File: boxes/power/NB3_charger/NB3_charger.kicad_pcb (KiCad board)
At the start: 2 copper layers, 65 x 150.1 mm, 58 parts, among them J1 Barrel_Jack-DC-5.5-2.1, J2 B4B-PH-K-S, J3 Conn_01x02_Pin, J4 Conn_01x02_Pin, J5 Conn_01x02_Pin, J6 Conn_01x02_Pin, Q1 PMOS_FDC658AP, SW1 SW_SPDT, SW2 SW_SPDT, T1 NTCG163JF103FT1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

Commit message: Work on NB3 Charger wiring
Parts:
- moved T1 99.1 mm to (128.9, 101.1)
- moved C1 43.0 mm to (177.7, 38.5)
- moved C10 43.0 mm to (162.0, 40.6)
- moved C11 43.0 mm to (163.7, 37.3)
- moved C12 43.0 mm to (167.7, 47.2)
- moved C13 43.0 mm to (170.2, 47.2)
- moved C14 43.0 mm to (170.2, 51.2)
- moved C15 43.0 mm to (167.7, 51.2)
- moved C16 43.0 mm to (173.7, 52.4)
- moved C2 43.0 mm to (175.2, 38.5)
- moved C3 43.0 mm to (180.2, 38.5)
- moved C4 43.0 mm to (180.2, 42.0)
- moved C5 43.0 mm to (177.7, 42.0)
- moved C6 43.0 mm to (175.2, 42.0)
- moved C7 43.0 mm to (161.5, 42.9)
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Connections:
- BT1 pad N: Net-(BT1-PadN) -> GND
- BT1 pad P: +BATT -> Net-(BT1-PadP)
- BT2 pad N: Net-(BT2-PadN) -> Net-(BT1-PadP)
- BT2 pad P: Net-(BT1-PadN) -> Net-(BT2-PadP)
- BT3 pad N: Net-(BT3-PadN) -> Net-(BT2-PadP)
- BT3 pad P: Net-(BT2-PadN) -> Net-(BT3-PadP)
- BT4 pad N: Net-(BT4-PadN) -> Net-(BT3-PadP)
- BT4 pad P: Net-(BT3-PadN) -> Net-(BT4-PadP)
- BT5 pad N: Net-(BT5-PadN) -> Net-(BT4-PadP)
- BT5 pad P: Net-(BT4-PadN) -> Net-(BT5-PadP)
- BT6 pad N: GND -> Net-(BT5-PadP)
- BT6 pad P: Net-(BT5-PadN) -> +BATT
- SW2 pad 1: Net-(SW2-A) -> GND
- SW2 pad 3: GND -> Net-(SW2-C)
- T1 pad 1: Net-(SW2-A) -> Net-(SW2-C)
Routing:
- net Net-(BT4-PadP): track 0.00 -> 19.8 mm
- net Net-(BT2-PadP): track 0.00 -> 19.8 mm
- net Net-(BT5-PadP): track 0.00 -> 17.0 mm
- net Net-(BT3-PadP): track 0.00 -> 17.0 mm
- net Net-(BT1-PadP): track 0.00 -> 17.0 mm
- net Net-(D3-K): track 0.00 -> 1.49 mm

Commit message: Work on NB3 charger PCB layout
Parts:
- added C20: 10uF 35v, Capacitor_SMD:C_0805_2012Metric, F.Cu at (87.6, 49.7)
- C18: value 10uF -> 10uF 35v
- moved CR2 56.3 mm to (120.5, 54.4), turned to -90 degrees
- moved C1 55.6 mm to (122.5, 32.2)
- moved C10 55.6 mm to (106.8, 34.2)
- moved C11 55.6 mm to (108.5, 30.9)
- moved C12 55.6 mm to (112.5, 40.9)
- moved C13 55.6 mm to (115.0, 40.9)
- moved C14 55.6 mm to (115.0, 44.9)
- moved C15 55.6 mm to (112.5, 44.9)
- moved C16 55.6 mm to (118.5, 46.0)
- moved C2 55.6 mm to (120.0, 32.2)
- moved C3 55.6 mm to (125.0, 32.2)
- moved C4 55.6 mm to (125.0, 35.7)
- moved C5 55.6 mm to (122.5, 35.7)
- moved C6 55.6 mm to (120.0, 35.7)
- moved C7 55.6 mm to (106.3, 36.5)
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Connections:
- J2 pad 1: +5V -> GND
- J2 pad 2: +5V -> GND
- J2 pad 3: GND -> +5V
- J2 pad 4: GND -> +5V
- SW1 pad 1: VDC -> +12V
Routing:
- net +12V: track 0.00 -> 193.3 mm
- net VDC: track 0.00 -> 92.2 mm, vias 0 -> 1
- net +BATT: track 0.00 -> 41.1 mm
- net +5V: track 31.0 -> 52.8 mm, vias 2 -> 0
- net Net-(Q1-G): track 0.00 -> 13.3 mm, vias 0 -> 2
- net Net-(U2-VSET): track 0.00 -> 2.26 mm
- net Net-(U2-ISET): track 0.00 -> 2.25 mm
- net Net-(U2-TMR): track 0.00 -> 1.05 mm
- net GND: vias 18 -> 12
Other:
- board size 65 x 150.1 mm -> 65 x 150 mm

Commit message: Preliminary routing of NB3_charger
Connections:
- U2 pad 10: (no net) -> GND
- U2 pad 11: (no net) -> GND
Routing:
- net Net-(SW1-B): track 1.88 -> 196.6 mm, vias 1 -> 4
- net Net-(U2-STAT): track 0.00 -> 187.4 mm, vias 0 -> 6
- net Net-(SW2-B): track 0.00 -> 186.0 mm, vias 0 -> 6
- net Net-(SW2-C): track 0.00 -> 77.1 mm, vias 0 -> 2
- net GND: track 9.67 -> 58.9 mm, vias 12 -> 28
- net +5V: track 52.8 -> 10.3 mm
- net VDC: track 92.2 -> 93.6 mm, vias 1 -> 2
- added copper zone on B.Cu, net GND
- added copper zone on F.Cu, net VDC
- removed copper zone on F.Cu, net +12V

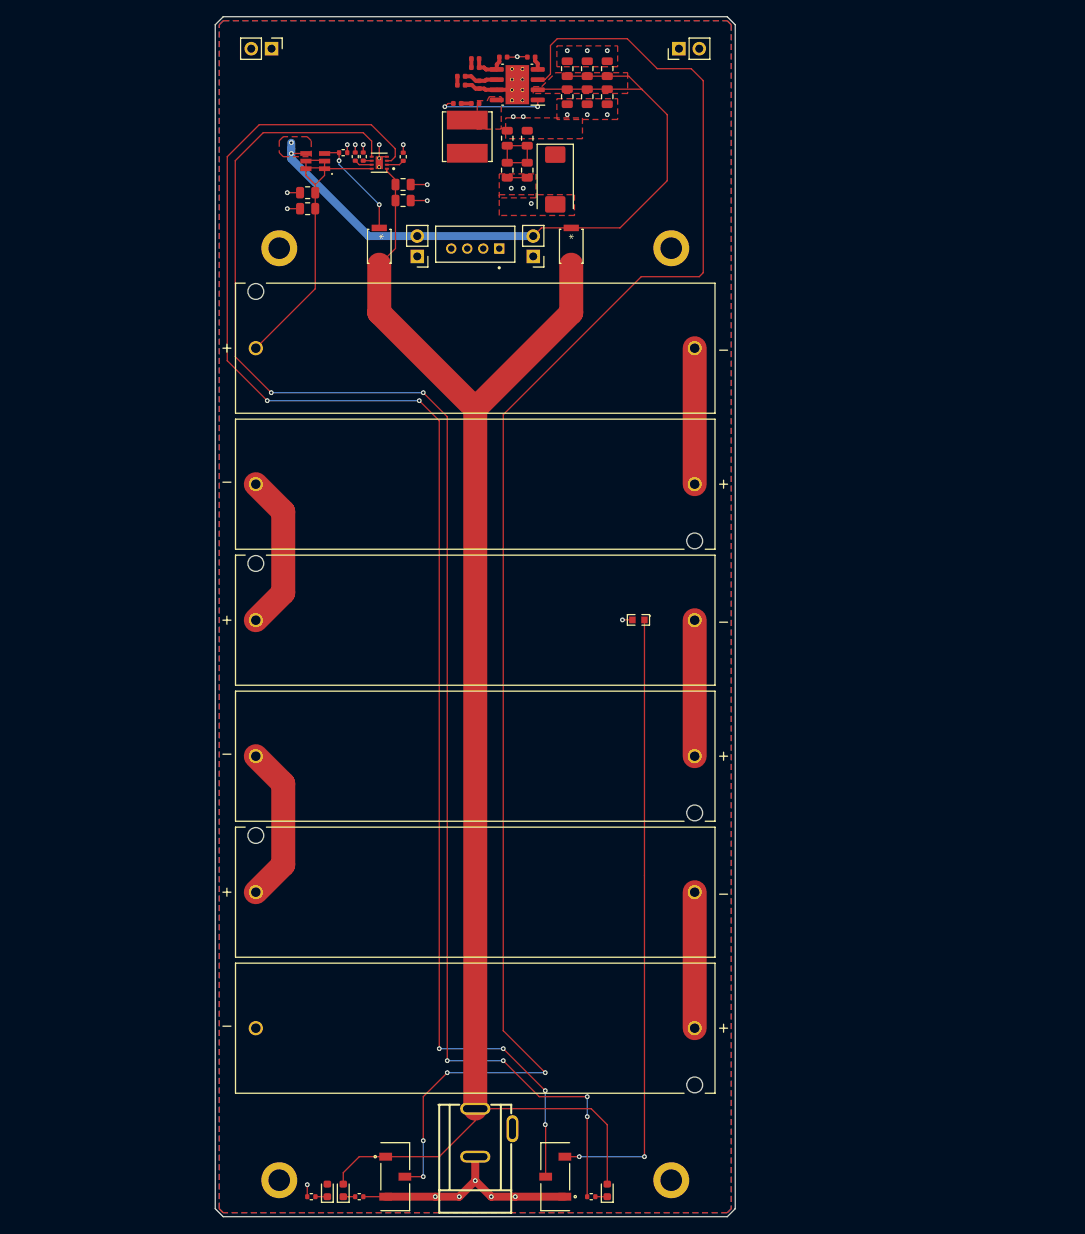
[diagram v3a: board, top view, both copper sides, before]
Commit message: Semi-final routing of NB3_Charger
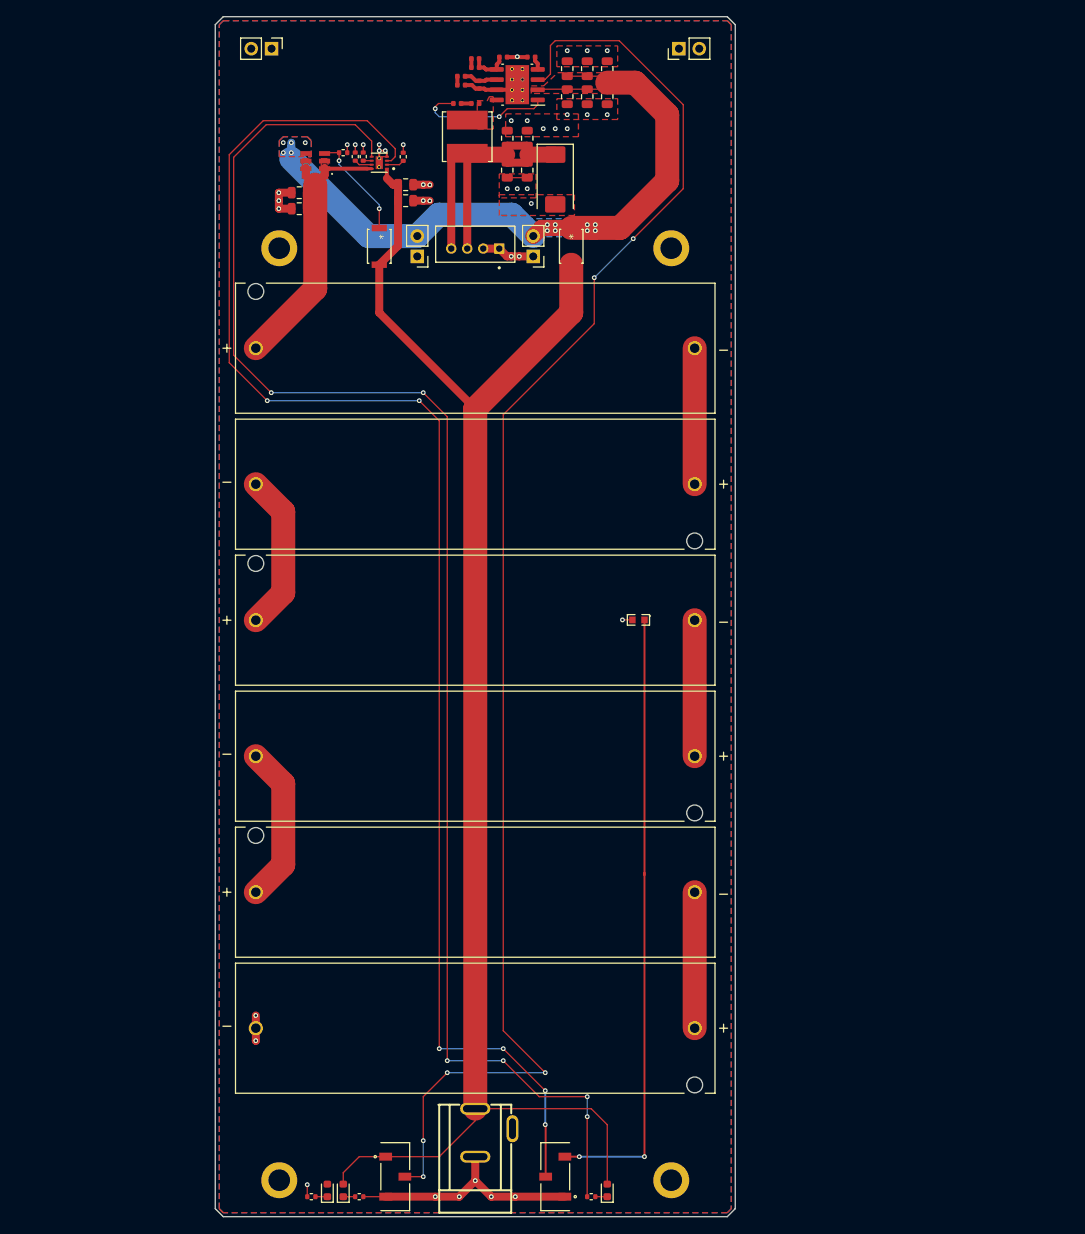
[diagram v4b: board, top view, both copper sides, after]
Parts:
- moved C18 1.05 mm to (86.5, 47.7)
- moved C20 1.05 mm to (86.5, 49.7)
- moved C17 0.32 mm to (99.8, 46.7)
- moved C19 0.32 mm to (99.8, 48.7)
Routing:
- net +5V: track 10.3 -> 44.8 mm
- net GND: track 58.9 -> 72.3 mm, vias 28 -> 41
- net Net-(SW1-B): track 196.6 -> 186.9 mm, vias 4 -> 6
- net +BATT: track 41.1 -> 36.6 mm
- net VDC: track 93.6 -> 89.2 mm, vias 2 -> 13
- net Net-(U1-BST): track 13.7 -> 17.4 mm
- net Net-(U2-STAT): track 187.4 -> 188.7 mm
- added copper zone on F.Cu, net +BATT
- added copper zone on B.Cu, net VDC

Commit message: Finish draft of NB3 Charger (submitted for Fab)
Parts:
- added G***: LOGO, NB3_charger:Logo_VK_15mm, B.Cu at (119.0, 134.9)
- BT1, BT2, BT3, BT4, BT5, BT6: footprint NB3_charger:AA_Battery_Holder_1028 -> NB3_charger:AA_Battery_Holder_BH-AA-A5BJ012
- moved T1 0.10 mm to (129.0, 101.1)
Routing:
- net Net-(BT4-PadP): track 19.8 -> 0.00 mm
- net Net-(BT4-Pad1): track 0.00 -> 19.8 mm
- net Net-(BT2-PadP): track 19.8 -> 0.00 mm
- net Net-(BT2-Pad1): track 0.00 -> 19.8 mm
- net Net-(BT5-PadP): track 17.0 -> 0.00 mm
- net Net-(BT5-Pad1): track 0.00 -> 17.0 mm
- net Net-(BT3-PadP): track 17.0 -> 0.00 mm
- net Net-(BT3-Pad1): track 0.00 -> 17.0 mm
- net Net-(BT1-PadP): track 17.0 -> 0.00 mm
- net Net-(BT1-Pad1): track 0.00 -> 17.0 mm
- net GND: track 72.3 -> 71.2 mm
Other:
- board text added: "0V|5V"
- board text added: "5V"
- board text added: "CHARGE"
- board text added: "DC-DC 5V Power Supply NiMH 6-Cell Charger"
- board text added: "For Research and Education ONLY"
- board text added: "GND VDC"
- board text added: "IN"
- board text added: "NB3 Charger"
- board text added: "NB3 Charger Rev. 0.0"
- board text added: "POWER"
- board text added: "Status"
